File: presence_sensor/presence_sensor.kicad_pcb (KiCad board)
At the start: 2 copper layers, 50 x 50 mm, 53 parts, among them J1 SG_UL, J10 SWITCH, J2 SG_UR, J3 SG_LL, J30 DIGITAL_OUT_5V, J31 OPTO_OUT, J4 SG_LR, J40 EXTERNAL_LOAD, J5 BRIDGE, J50 12V_IN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

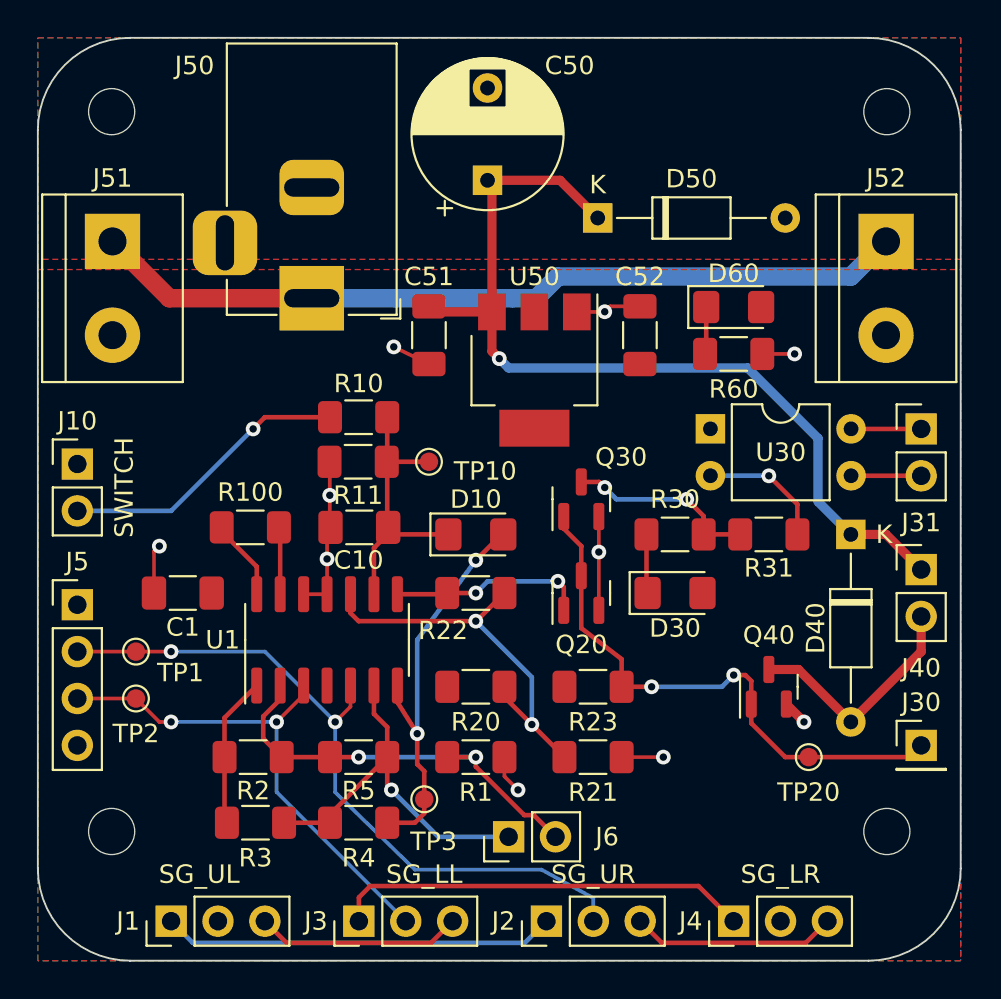
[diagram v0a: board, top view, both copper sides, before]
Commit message: Remove unneeded testpoints
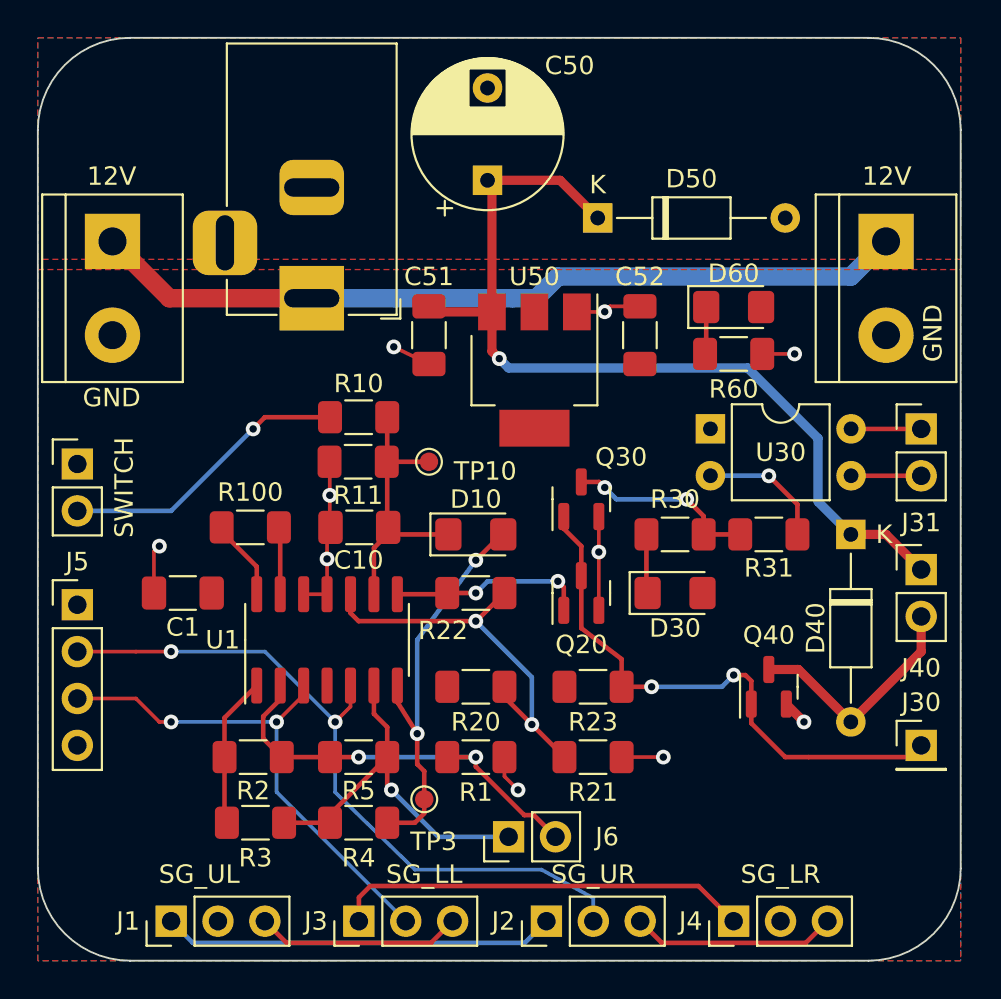
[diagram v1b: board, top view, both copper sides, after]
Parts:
- removed REF** (x4): MountingHole_2.5mm, MountingHole:MountingHole_2.5mm
- removed TP1: SenseHigh, TestPoint:TestPoint_Pad_D1.0mm
- removed TP2: SenseLow, TestPoint:TestPoint_Pad_D1.0mm
- removed TP20: Presence, TestPoint:TestPoint_Pad_D1.0mm
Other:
- board text added: "12V"
- board text added: "GND"
- board text added: "Presence sensor v1.0 September 2023"

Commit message: Minor rerouting for beauty
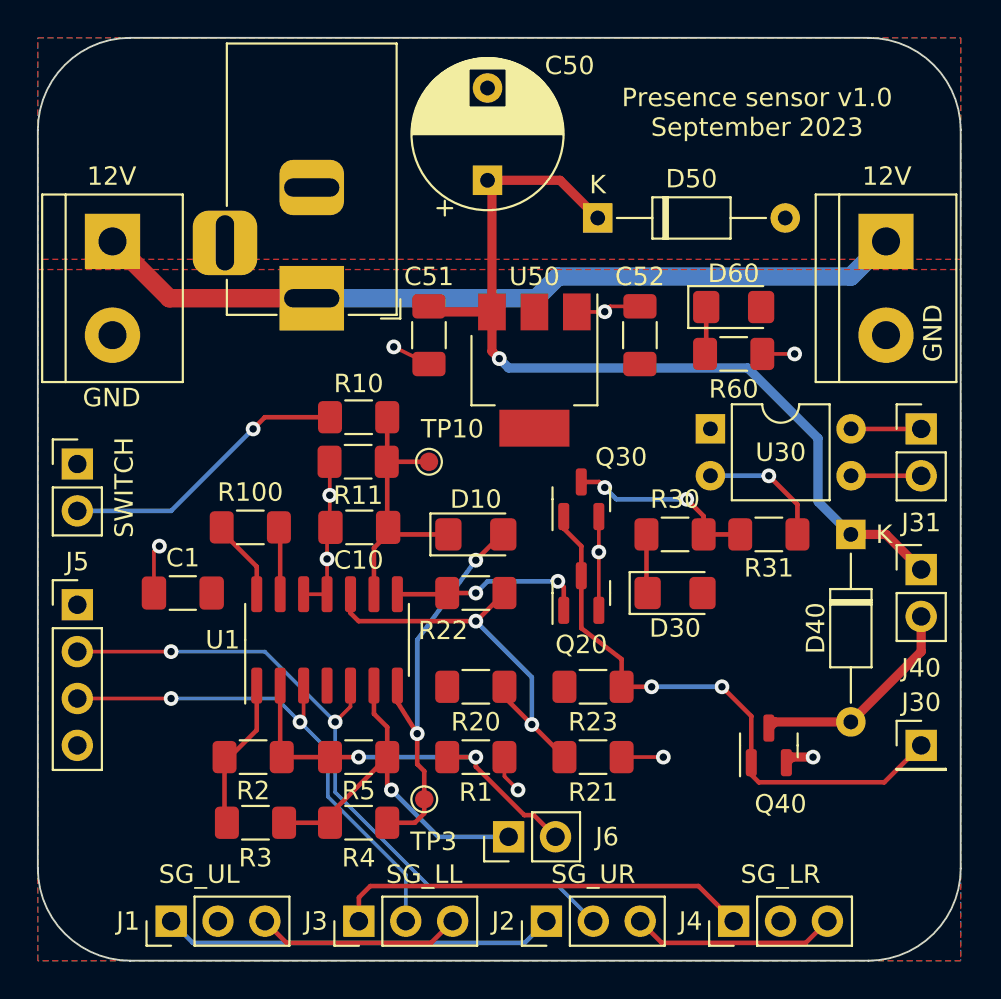
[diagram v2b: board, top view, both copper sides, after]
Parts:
- moved Q40 3.17 mm to (89.6, 88.3)
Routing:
- net PRESENCE: track 30.6 -> 31.8 mm
- net Net-(D40-Pad2): track 12.9 -> 11.9 mm
- net Net-(J6-Pad2): track 23.1 -> 22.4 mm

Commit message: Add labels on silkscreen for outputs. Minor rerouting for beauty.
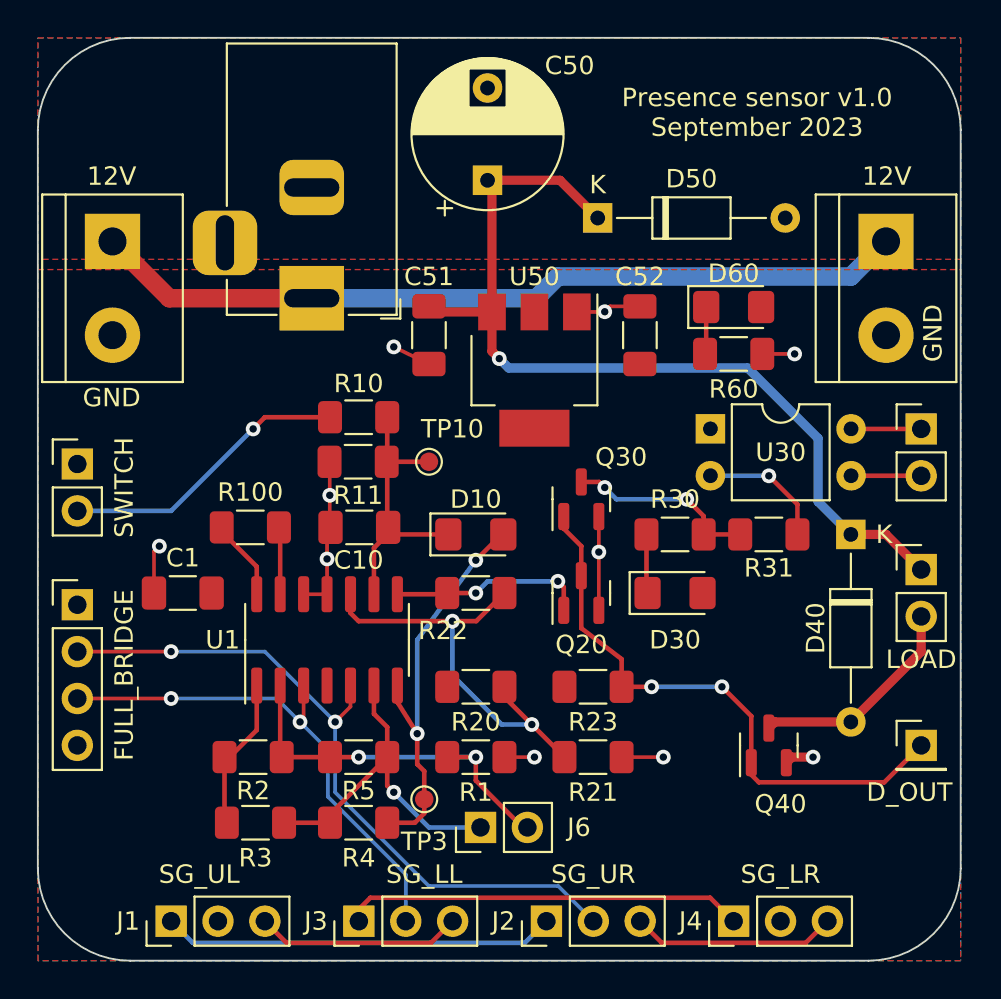
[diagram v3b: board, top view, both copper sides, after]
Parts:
- J30: value DIGITAL_OUT_5V -> D_OUT
- J40: value EXTERNAL_LOAD -> LOAD
- J5: value BRIDGE -> FULL_BRIDGE
- moved J6 1.61 mm to (74.0, 92.8)
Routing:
- net Net-(J6-Pad1): track 20.8 -> 19.0 mm
- net Net-(R20-Pad2): track 22.2 -> 23.7 mm
- net Net-(J6-Pad2): track 22.4 -> 21.1 mm
- net Net-(J3-Pad1): track 22.6 -> 21.7 mm

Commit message: Move power indicator LED.
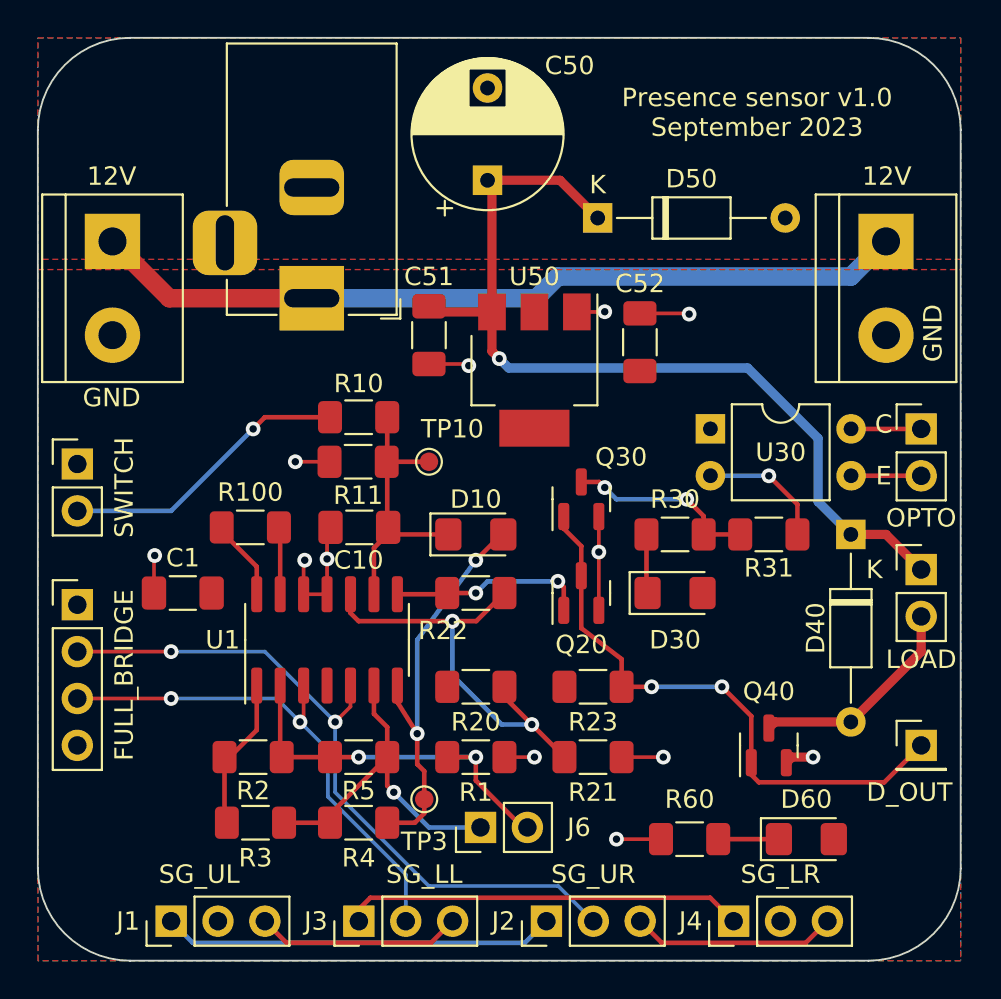
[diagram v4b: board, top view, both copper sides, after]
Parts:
- J31: value OPTO_OUT -> OPTO
- moved D60 29.1 mm to (91.6, 93.4)
- moved R60 26.4 mm to (85.3, 93.4), turned to 180 degrees
- moved C52 0.38 mm to (82.6, 66.5)
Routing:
- net E-: track 28.4 -> 29.8 mm, vias 10 -> 12
- net Net-(D60-Pad1): track 2.57 -> 3.29 mm
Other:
- board text added: "C"
- board text added: "E"
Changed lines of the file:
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@@
     (property "Sheetname" "")
     (attr smd)
-    (fp_text reference "Q40" (at -3.175 0.635 180) (layer "F.SilkS")
+    (fp_text reference "Q40" (at 2.921 0 180) (layer "F.SilkS")
       (effects (font (size 1 1) (thickness 0.15)))
     )
@@
       (effects (font (size 1 1) (thickness 0.15)))
     )
-    (fp_text value "OPTO_OUT" (at 0 4.87) (layer "F.Fab")
+    (fp_text value "OPTO" (at 0 4.826) (layer "F.SilkS")
       (effects (font (size 1 1) (thickness 0.15)))
     )
@@
       (effects (font (size 1 1) (thickness 0.15)))
     )
-    (fp_text user "K" (at 0 -1.8) (layer "F.SilkS")
+    (fp_text user "K" (at 1.905 -1.27) (layer "F.SilkS")
       (effects (font (size 1 1) (thickness 0.15)))
     )
@@
   )
   (footprint "LED_SMD:LED_1206_3216Metric_Pad1.42x1.75mm_HandSolder" (layer "F.Cu")
-    (at 87.7 64.586)
+    (at 91.637 93.415)
     (descr "LED SMD 1206 (3216 Metric), square (rectangular) end terminal, IPC_7351 nominal, (Body size source: http://www.tortai-tech.com/upload/download/2011102023233369053.pdf), generated with kicad-footprint-generator")
     (tags "LED handsolder")
@@
     (property "Sheetname" "")
     (attr smd)
-    (fp_text reference "D60" (at 0 -1.82) (layer "F.SilkS")
+    (fp_text reference "D60" (at 0 -2.159) (layer "F.SilkS")
       (effects (font (size 1 1) (thickness 0.15)))
     )
@@
   )
   (footprint "Resistor_SMD:R_1206_3216Metric_Pad1.30x1.75mm_HandSolder" (layer "F.Cu")
-    (at 87.7 67.126)
+    (at 85.313 93.415 180)
     (descr "Resistor SMD 1206 (3216 Metric), square (rectangular) end terminal, IPC_7351 nominal with elongated pad for handsoldering. (Body size source: IPC-SM-782 page 72, https://www.pcb-3d.com/wordpress/wp-content/uploads/ipc-sm-782a_amendment_1_and_2.pdf), generated with kicad-footprint-generator")
     (tags "resistor handsolder")
@@
     (property "Sheetname" "")
     (attr smd)
-    (fp_text reference "R60" (at 0 1.905 180) (layer "F.SilkS")
+    (fp_text reference "R60" (at 0 2.159) (layer "F.SilkS")
       (effects (font (size 1 1) (thickness 0.15)))
     )
@@
     (fp_line (start 1.6 0.8) (end -1.6 0.8) (layer "F.Fab") (width 0.1))
     (fp_line (start -1.6 -0.8) (end 1.6 -0.8) (layer "F.Fab") (width 0.1))
-    (pad "1" smd roundrect (at -1.55 0) (size 1.3 1.75) (layers "F.Cu" "F.Paste" "F.Mask") (roundrect_rratio 0.192308)
+    (pad "1" smd roundrect (at -1.55 0 180) (size 1.3 1.75) (layers "F.Cu" "F.Paste" "F.Mask") (roundrect_rratio 0.192308)
       (net 28 "Net-(D60-Pad1)") (pintype "passive"))
-    (pad "2" smd roundrect (at 1.55 0) (size 1.3 1.75) (layers "F.Cu" "F.Paste" "F.Mask") (roundrect_rratio 0.192308)
+    (pad "2" smd roundrect (at 1.55 0 180) (size 1.3 1.75) (layers "F.Cu" "F.Paste" "F.Mask") (roundrect_rratio 0.192308)
       (net 2 "E-") (pintype "passive"))
     (model "${KICAD6_3DMODEL_DIR}/Resistor_SMD.3dshapes/R_1206_3216Metric.wrl"
@@
   )
   (footprint "Capacitor_SMD:C_1206_3216Metric_Pad1.33x1.80mm_HandSolder" (layer "F.Cu")
-    (at 82.62 66.11 90)
+    (at 82.62 66.491 90)
     (descr "Capacitor SMD 1206 (3216 Metric), square (rectangular) end terminal, IPC_7351 nominal with elongated pad for handsoldering. (Body size source: IPC-SM-782 page 76, https://www.pcb-3d.com/wordpress/wp-content/uploads/ipc-sm-782a_amendment_1_and_2.pdf), generated with kicad-footprint-generator")
     (tags "capacitor handsolder")
@@
   (gr_line (start 55 50) (end 95 50) (layer "Edge.Cuts") (width 0.1))
   (gr_line (start 50 95) (end 50 55) (layer "Edge.Cuts") (width 0.1))
+  (gr_text "C" (at 95.828 70.936) (layer "F.SilkS")
+    (effects (font (size 1 1) (thickness 0.15)))
+  )
   (gr_text "Presence sensor v1.0\nSeptember 2023" (at 88.97 54.045) (layer "F.SilkS")
     (effects (font (size 1 1) (thickness 0.15)))
@@
     (effects (font (size 1 1) (thickness 0.15)))
   )
+  (gr_text "E" (at 95.828 73.73) (layer "F.SilkS")
+    (effects (font (size 1 1) (thickness 0.15)))
+  )
   (segment (start 81.63 88.97) (end 83.89 88.97) (width 0.2) (layer "F.Cu") (net 2))
-  (segment (start 65.8175 76.905) (end 65.8175 74.7845) (width 0.2) (layer "F.Cu") (net 2))
+  (segment (start 83.763 93.415) (end 81.35 93.415) (width 0.2) (layer "F.Cu") (net 2))
+  (segment (start 56.2925 78.0865) (end 56.2925 80.08) (width 0.2) (layer "F.Cu") (net 2))
+  (segment (start 64.4 78.361) (end 64.459 78.302) (width 0.2) (layer "F.Cu") (net 2))
   (segment (start 90.555 89.2725) (end 90.8575 88.97) (width 0.5) (layer "F.Cu") (net 2))
-  (segment (start 82.62 64.5475) (end 81.0075 64.5475) (width 0.2) (layer "F.Cu") (net 2))
+  (segment (start 56.331 78.048) (end 56.2925 78.0865) (width 0.2) (layer "F.Cu") (net 2))
+  (segment (start 85.2485 64.9285) (end 85.287 64.967) (width 0.2) (layer "F.Cu") (net 2))
+  (segment (start 73.349 67.761) (end 73.2605 67.6725) (width 0.2) (layer "F.Cu") (net 2))
   (segment (start 64.4 80.145) (end 65.67 80.145) (width 0.2) (layer "F.Cu") (net 2))
   (segment (start 79.205 64.85) (end 80.705 64.85) (width 0.2) (layer "F.Cu") (net 2))
-  (segment (start 56.2925 80.08) (end 56.2925 77.8325) (width 0.2) (layer "F.Cu") (net 2))
   (segment (start 80.395 77.86) (end 80.395 81.0175) (width 0.2) (layer "F.Cu") (net 2))
+  (segment (start 82.62 64.9285) (end 82.5315 64.84) (width 0.2) (layer "F.Cu") (net 2))
   (segment (start 76.905 88.97) (end 75.28 88.97) (width 0.2) (layer "F.Cu") (net 2))
+  (segment (start 65.804 72.968) (end 63.951 72.968) (width 0.2) (layer "F.Cu") (net 2))
   (segment (start 90.8575 88.97) (end 92 88.97) (width 0.5) (layer "F.Cu") (net 2))
-  (segment (start 69.285 66.745) (end 71.19 67.6725) (width 0.2) (layer "F.Cu") (net 2))
+  (segment (start 64.4 80.145) (end 64.4 78.361) (width 0.2) (layer "F.Cu") (net 2))
   (segment (start 65.8175 73.7425) (end 65.83 73.73) (width 0.2) (layer "F.Cu") (net 2))
+  (segment (start 82.62 64.9285) (end 85.2485 64.9285) (width 0.2) (layer "F.Cu") (net 2))
   (segment (start 80.705 64.85) (end 80.715 64.84) (width 0.2) (layer "F.Cu") (net 2))
-  (segment (start 65.8175 74.7845) (end 65.8175 73.7425) (width 0.2) (layer "F.Cu") (net 2))
-  (segment (start 56.2925 77.8325) (end 56.585 77.54) (width 0.2) (layer "F.Cu") (net 2))
-  (segment (start 91.002 67.126) (end 89.25 67.126) (width 0.2) (layer "F.Cu") (net 2))
   (segment (start 65.67 77.0525) (end 65.8175 76.905) (width 0.2) (layer "F.Cu") (net 2))
+  (segment (start 73.2605 67.6725) (end 71.19 67.6725) (width 0.2) (layer "F.Cu") (net 2))
   (segment (start 65.67 80.145) (end 65.67 78.234) (width 0.2) (layer "F.Cu") (net 2))
   (segment (start 80.395 75.9375) (end 80.395 77.86) (width 0.2) (layer "F.Cu") (net 2))
   (segment (start 65.67 78.234) (end 65.67 77.0525) (width 0.2) (layer "F.Cu") (net 2))
-  (segment (start 81.0075 64.5475) (end 80.715 64.84) (width 0.2) (layer "F.Cu") (net 2))
+  (via (at 81.35 93.415) (size 0.8) (drill 0.4) (layers "F.Cu" "B.Cu") (net 2))
+  (via (at 85.287 64.967) (size 0.8) (drill 0.4) (layers "F.Cu" "B.Cu") (net 2))
   (via (at 83.89 88.97) (size 0.8) (drill 0.4) (layers "F.Cu" "B.Cu") (net 2))
   (via (at 92 88.97) (size 0.8) (drill 0.4) (layers "F.Cu" "B.Cu") (net 2))
-  (via (at 65.8175 74.7845) (size 0.8) (drill 0.4) (layers "F.Cu" "B.Cu") (net 2))
-  (via (at 56.585 77.54) (size 0.8) (drill 0.4) (layers "F.Cu" "B.Cu") (net 2))
+  (via (at 56.331 78.048) (size 0.8) (drill 0.4) (layers "F.Cu" "B.Cu") (net 2))
   (via (at 80.715 64.84) (size 0.8) (drill 0.4) (layers "F.Cu" "B.Cu") (net 2))
   (via (at 76.905 88.97) (size 0.8) (drill 0.4) (layers "F.Cu" "B.Cu") (net 2))
   (via (at 65.67 78.234) (size 0.8) (drill 0.4) (layers "F.Cu" "B.Cu") (net 2))
-  (via (at 91.002 67.126) (size 0.8) (drill 0.4) (layers "F.Cu" "B.Cu") (net 2))
-  (via (at 69.285 66.745) (size 0.8) (drill 0.4) (layers "F.Cu" "B.Cu") (net 2))
+  (via (at 63.951 72.968) (size 0.8) (drill 0.4) (layers "F.Cu" "B.Cu") (net 2))
+  (via (at 64.459 78.302) (size 0.8) (drill 0.4) (layers "F.Cu" "B.Cu") (net 2))
+  (via (at 73.349 67.761) (size 0.8) (drill 0.4) (layers "F.Cu" "B.Cu") (net 2))
   (via (at 80.395 77.86) (size 0.8) (drill 0.4) (layers "F.Cu" "B.Cu") (net 2))
   (segment (start 68.93 72.942) (end 68.904 72.968) (width 0.25) (layer "F.Cu") (net 3))
@@
   (segment (start 61.86 78.65) (end 60.115 76.905) (width 0.25) (layer "F.Cu") (net 27))
   (segment (start 61.86 80.145) (end 61.86 78.65) (width 0.25) (layer "F.Cu") (net 27))
-  (segment (start 86.2125 64.586) (end 86.2125 67.0635) (width 0.25) (layer "F.Cu") (net 28))
-  (segment (start 86.2125 67.0635) (end 86.15 67.126) (width 0.25) (layer "F.Cu") (net 28))
+  (segment (start 86.863 93.415) (end 90.1495 93.415) (width 0.25) (layer "F.Cu") (net 28))
   (zone (net 1) (net_name "E+") (layer "F.Cu") (hatch edge 0.508)
     (connect_pads (clearance 0.508))
